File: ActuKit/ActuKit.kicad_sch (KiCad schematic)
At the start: 8 parts, among them J1 Conn_01x04_Pin, J2 Conn_01x04_Pin, Q1 2SC1815, U1 LD14-002, U2 BD6211

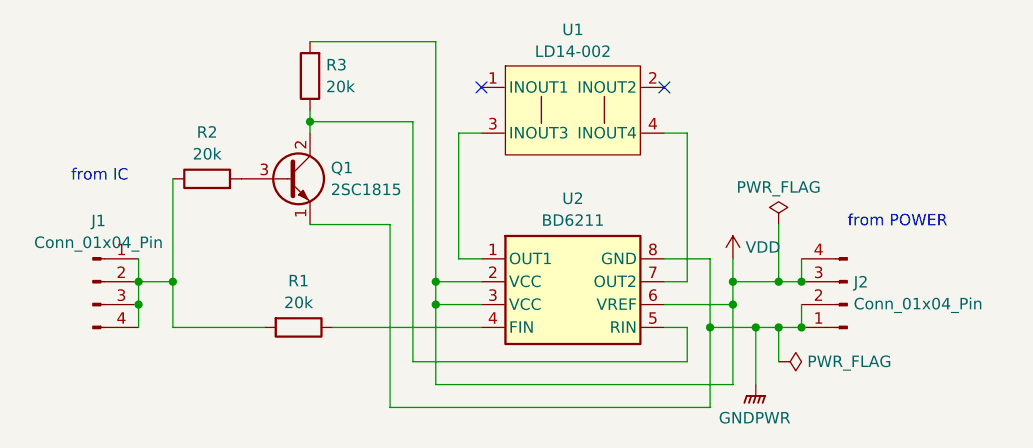
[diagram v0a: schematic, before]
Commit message: [ActuKit] ミルピンのガイド用シルクの追加
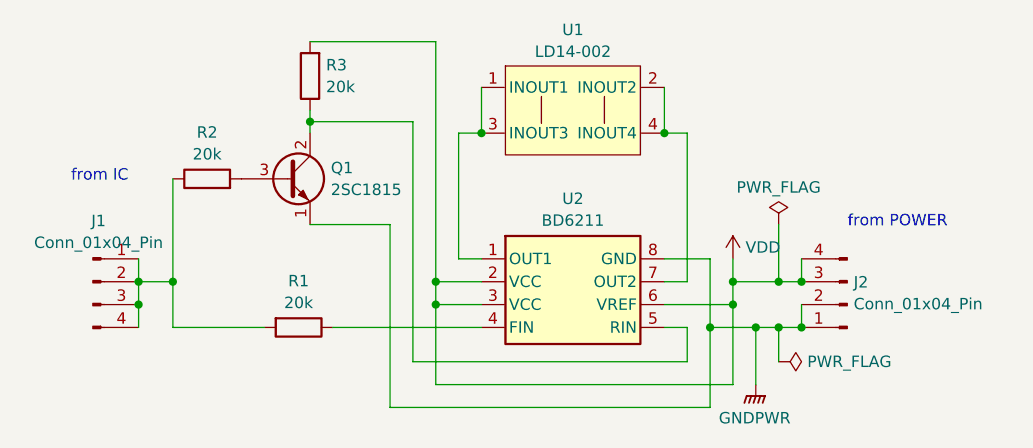
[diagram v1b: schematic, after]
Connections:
- net at U1.3 (INOUT3), U2.1 (OUT1): now also U1.1 (INOUT1)
- net at U1.4 (INOUT4), U2.7 (OUT2): now also U1.2 (INOUT2)
- no-connect marks 2 -> 0
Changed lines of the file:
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@@
+	)
+	(junction
+		(at 127 87.63)
+		(diameter 0)
+		(color 0 0 0 0)
 	)
 	(junction
@@
 	)
 	(junction
+		(at 147.32 87.63)
+		(diameter 0)
+		(color 0 0 0 0)
+	)
+	(junction
 		(at 152.4 109.22)
 		(diameter 0)
@@
 		(color 0 0 0 0)
 	)
-	(no_connect
-		(at 147.32 82.55)
-	)
-	(no_connect
-		(at 127 82.55)
-	)
 	(wire
 		(pts
@@
 	(wire
 		(pts
+			(xy 127 82.55) (xy 127 87.63)
+		)
+		(stroke
+			(width 0)
+			(type default)
+		)
+	)
+	(wire
+		(pts
 			(xy 116.84 118.11) (xy 116.84 97.79)
 		)
@@
 		)
 		(stroke
+			(width 0)
+			(type default)
+		)
+	)
+	(wire
+		(pts
+			(xy 147.32 82.55) (xy 147.32 87.63)
+		)
+		(stroke
